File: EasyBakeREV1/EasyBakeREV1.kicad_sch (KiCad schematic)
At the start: 28 parts, among them U1 MIC5219-3.3YM5, U2 USBLC6-2SC6, U3 PCA9702, Y1 12MHz

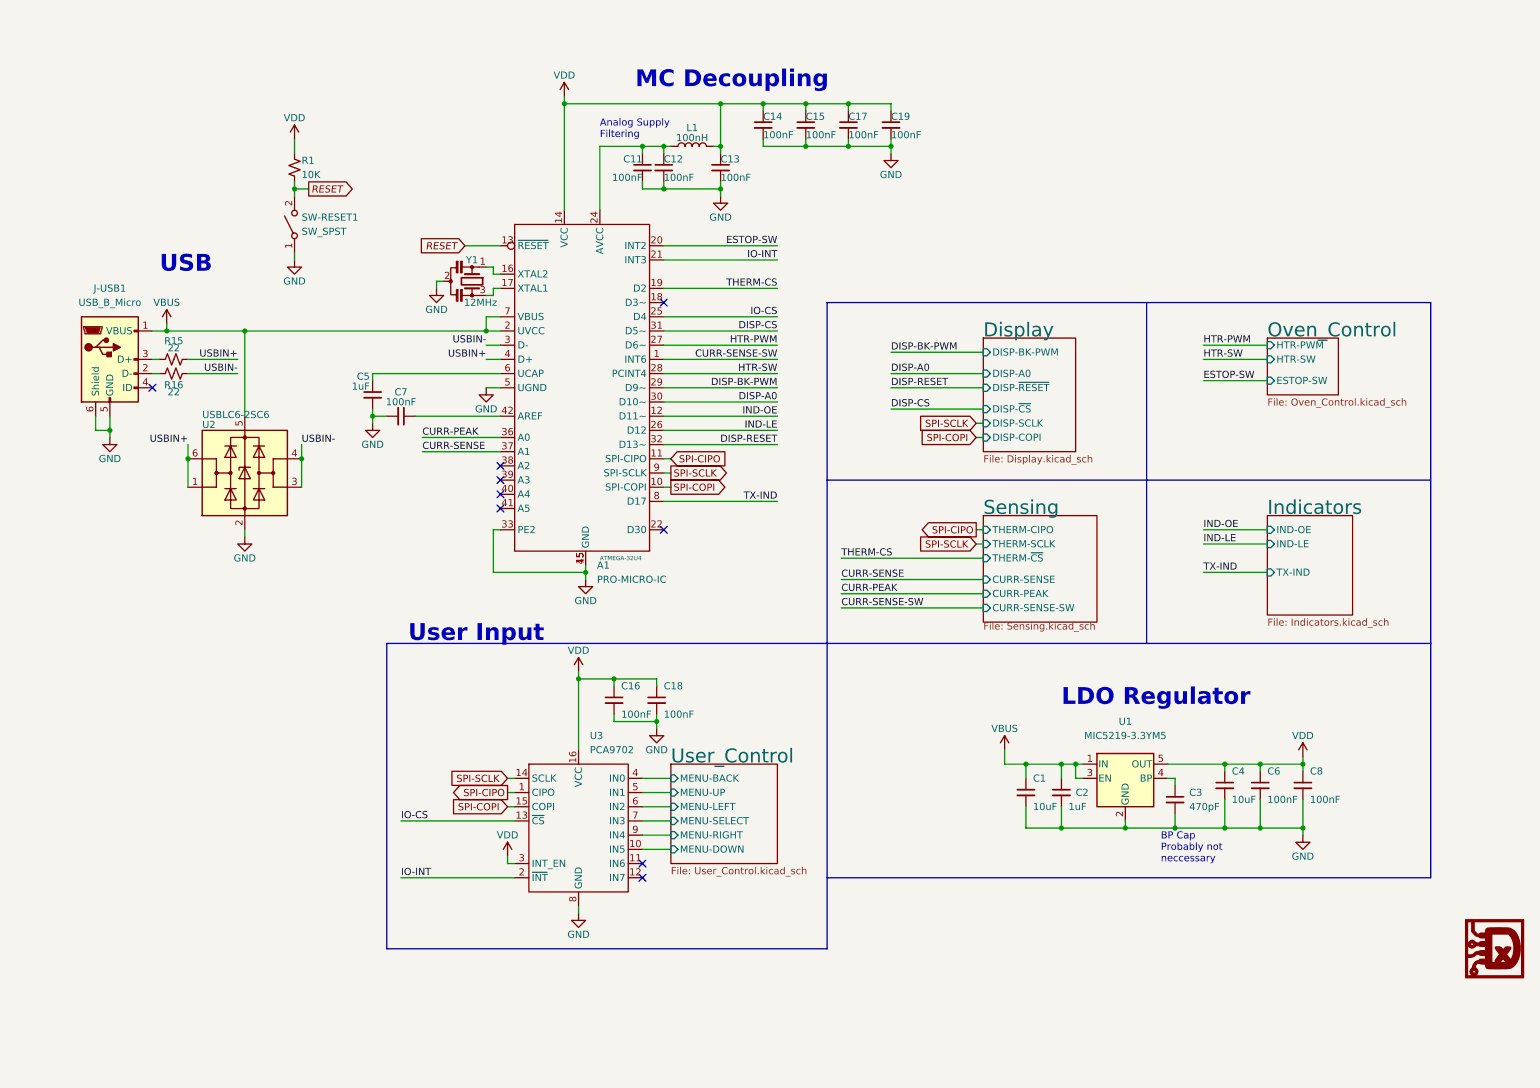
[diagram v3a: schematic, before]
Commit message: Change main pwr to 3.3 due to USB issues
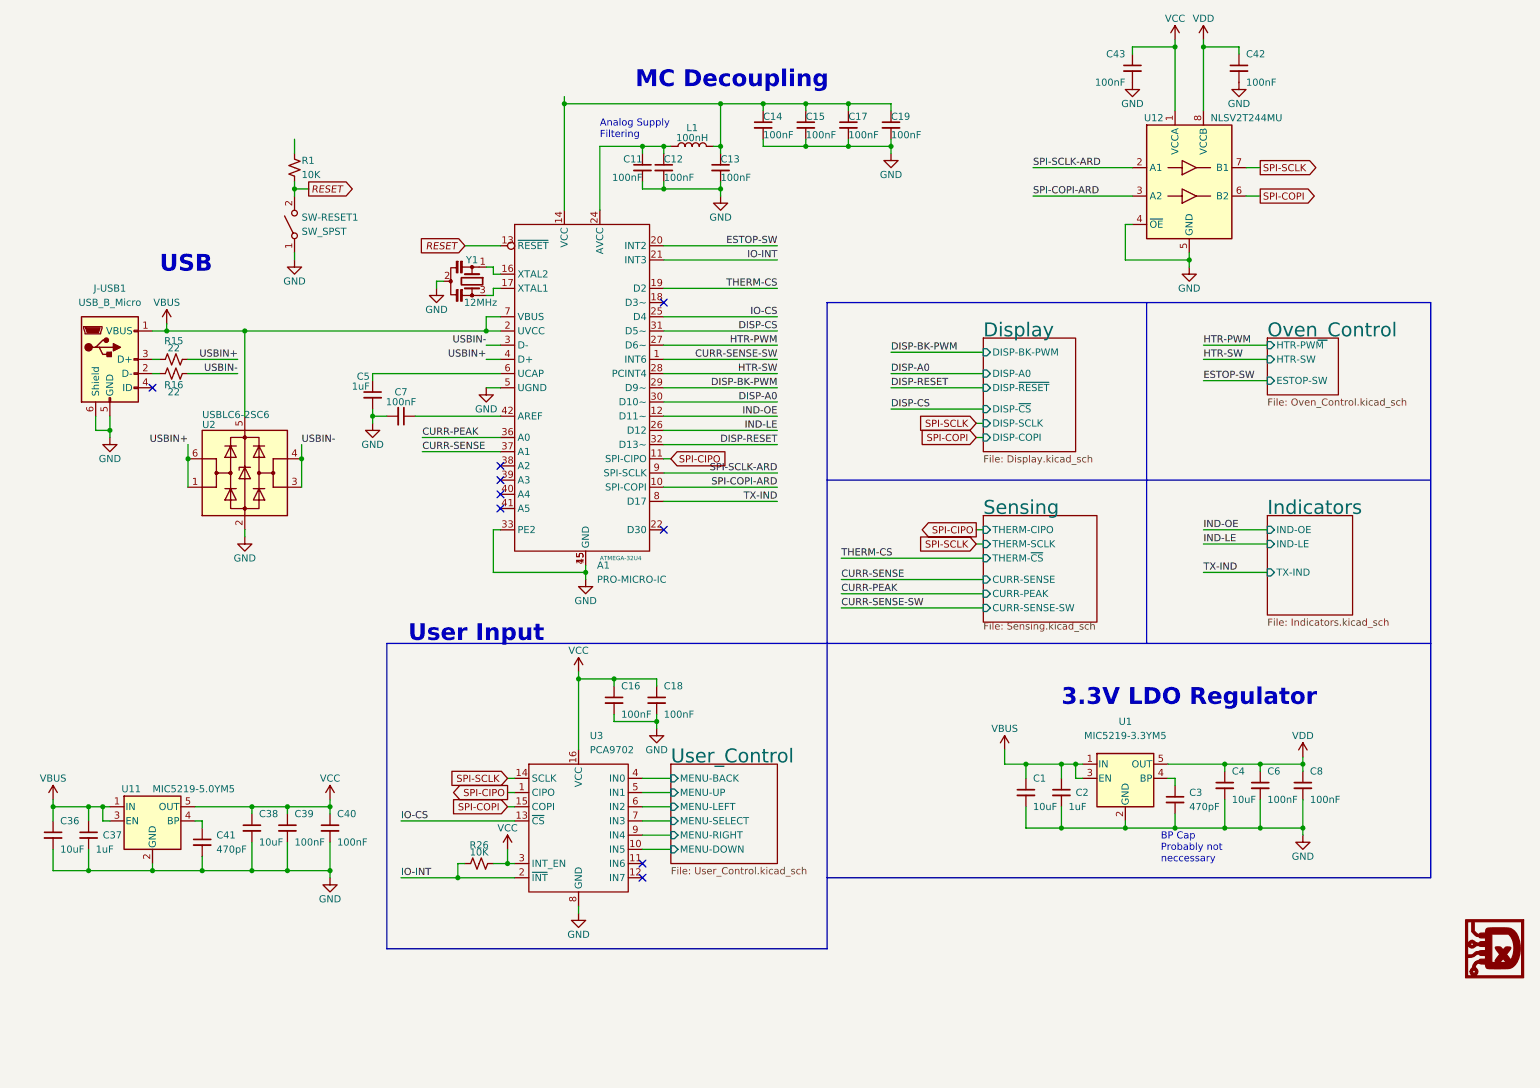
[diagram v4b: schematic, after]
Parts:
- added C36, C38: 10uF, Capacitor_SMD:C_1210_3225Metric, symbol Device:C_Small
- added C37: 1uF, Capacitor_SMD:C_1210_3225Metric, symbol Device:C_Small
- added C39, C40: 100nF, Capacitor_SMD:C_0603_1608Metric, symbol Device:C_Small
- added C41: 470pF, Capacitor_SMD:C_0603_1608Metric, symbol Device:C_Small
- added C42, C43: 100nF, Capacitor_SMD:C_0805_2012Metric, symbol Device:C_Small
- added R26: 10K, Resistor_SMD:R_0603_1608Metric, symbol Device:R_Small_US
- added U11: MIC5219-5.0YM5, Package_TO_SOT_SMD:SOT-23-5, symbol Regulator_Linear:MIC5219-5.0YM5
- added U12: NLSV2T244MU, Package_DFN_QFN:OnSemi_UDFN-8_1.2x1.8mm_P0.4mm, symbol Logic_LevelTranslator:NLSV2T244MU
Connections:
- net GND: now also C36.2, C37.2, C38.2, C39.2, C40.2, C41.2, C42.2, C43.2, U11.2 (GND), U12.4 (~{OE}), U12.5 (GND)
- net IO-INT: now also R26.1
- net SPI-COPI: now also U12.6 (B2); no longer A1.10 (PB2)
- net SPI-SCLK: now also U12.7 (B1); no longer A1.9 (PB1)
- net VBUS: now also C36.1, C37.1, U11.1 (IN), U11.3 (EN)
- net VCC: now also C38.1, C39.1, C40.1, C43.1, R26.2, U11.5 (OUT), U12.1 (VCCA); no longer C4.1, C6.1, C8.1, R1.1, U1.5 (OUT)
- new net: C41.1, U11.4 (BP)
- new net SPI-COPI-ARD: A1.10 (PB2), U12.3 (A2)
- new net SPI-SCLK-ARD: A1.9 (PB1), U12.2 (A1)
- new net VDD: C4.1, C42.1, C6.1, C8.1, U1.5 (OUT), U12.8 (VCCB)
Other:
- note added: "3.3V LDO Regulator"
- note removed: "LDO Regulator"

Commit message: Replaced MCU - started layout
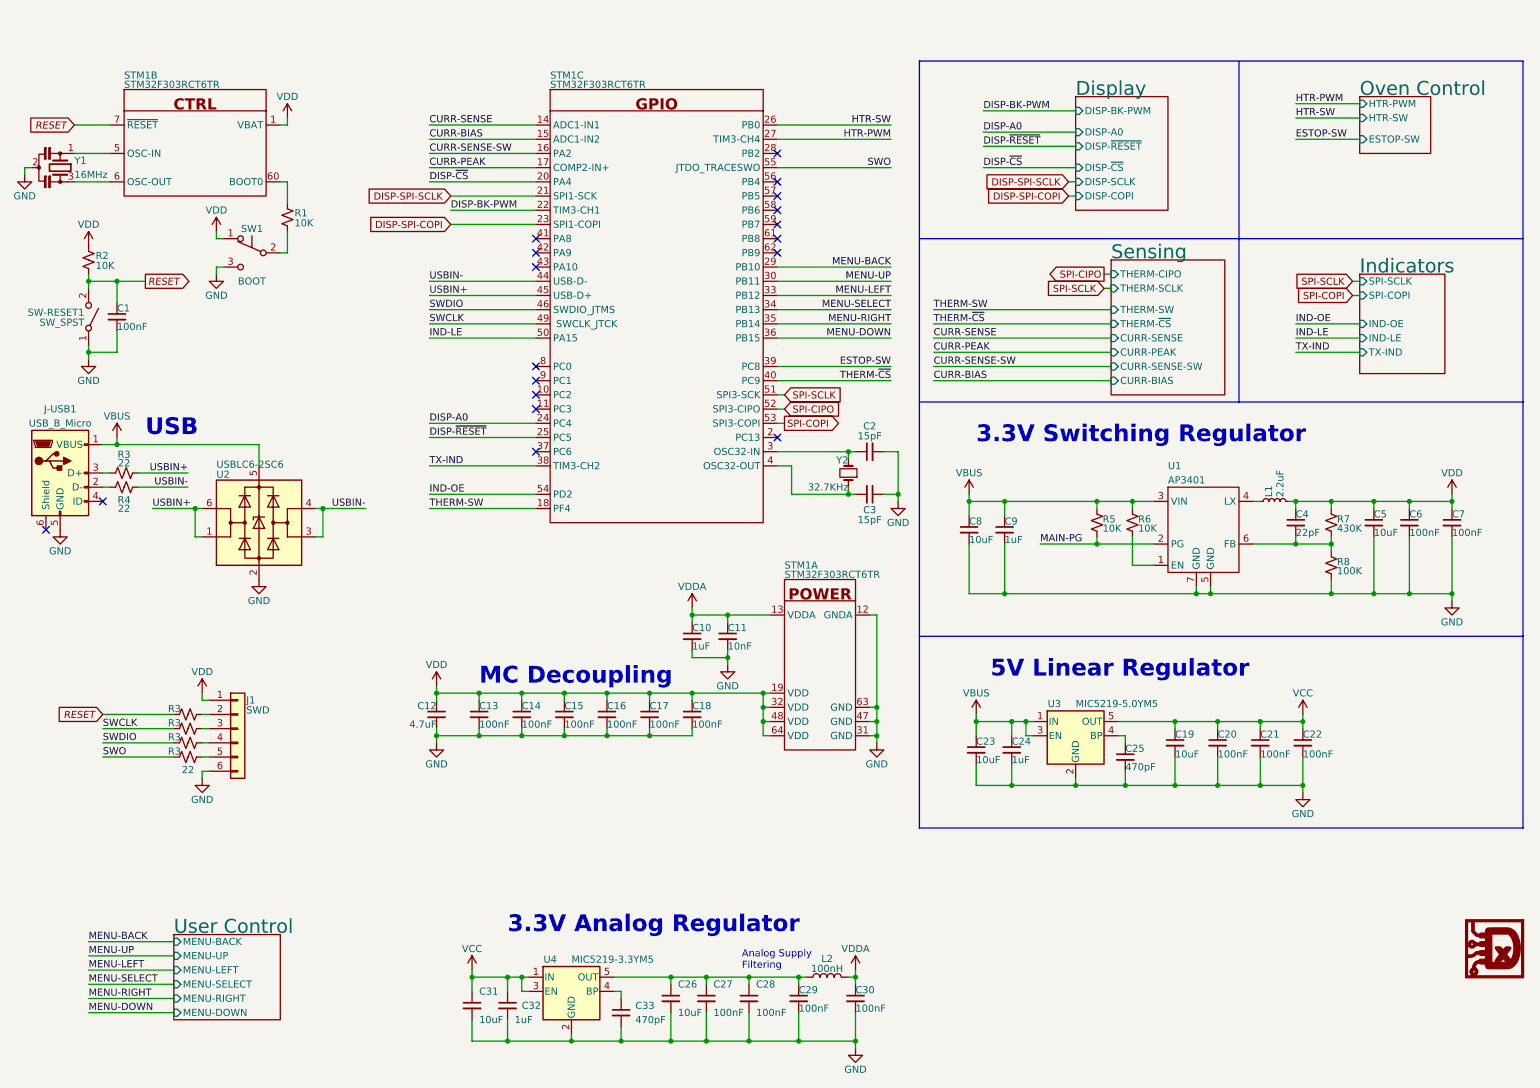
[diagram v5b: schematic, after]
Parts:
- removed A1: PRO-MICRO-IC, Daxxn_Packages:QFN-44-1EP_7x7mm_P0.5mm_EP4.8x4.8mm, symbol Daxxn_Arduino:PRO-MICRO-IC
- removed C42, C43: 100nF, Capacitor_SMD:C_0805_2012Metric, symbol Device:C_Small
- removed C5: 1uF, Capacitor_SMD:C_0805_2012Metric, symbol Device:C_Small
- removed C7: 100nF, Capacitor_SMD:C_0603_1608Metric, symbol Device:C_Small
- removed R26: 10K, Resistor_SMD:R_0603_1608Metric, symbol Device:R_Small_US
- removed U1: MIC5219-3.3YM5, Package_TO_SOT_SMD:SOT-23-5, symbol Regulator_Linear:MIC5219-3.3YM5
- removed U12: NLSV2T244MU, Package_DFN_QFN:OnSemi_UDFN-8_1.2x1.8mm_P0.4mm, symbol Logic_LevelTranslator:NLSV2T244MU
- removed U3: PCA9702, Package_SO:SSOP-16_4.4x5.2mm_P0.65mm, symbol Daxxn_IC:PCA9702
- added C1, C22, C27, C28: 100nF, Capacitor_SMD:C_0402_1005Metric, symbol Device:C_Small
- added C10, C32: 1uF, Capacitor_SMD:C_0805_2012Metric, symbol Device:C_Small
- added C12: 4.7uF, Capacitor_SMD:C_0805_2012Metric, symbol Device:C_Small
- added C2, C3: 15pF, Capacitor_SMD:C_0402_1005Metric, symbol Daxxn_Device:C
- added C26, C31: 10uF, Capacitor_SMD:C_1210_3225Metric, symbol Device:C_Small
- added C33: 470pF, Capacitor_SMD:C_0603_1608Metric, symbol Device:C_Small
- added J1: SWD, Connector_PinHeader_1.27mm:PinHeader_1x06_P1.27mm_Vertical, symbol Connector_Generic:Conn_01x06
- added L1: 2.2uF, Daxxn_Passives:LQH3NPN, symbol Daxxn_Device:L
- added R1: 10K, Resistor_SMD:R_0402_1005Metric, symbol Device:R_Small_US
- added R3 (x4): 22, Resistor_SMD:R_0402_1005Metric, symbol Device:R_Small_US
- added R5, R6: 10K, Resistor_SMD:R_0402_1005Metric, symbol Daxxn_Device:R
- added R7: 430K, Resistor_SMD:R_0402_1005Metric, symbol Daxxn_Device:R
- added R8: 100K, Resistor_SMD:R_0402_1005Metric, symbol Daxxn_Device:R
- added STM1: STM32F303RCT6TR, Package_QFP:LQFP-64_10x10mm_P0.5mm, symbol Daxxn_STMicros:STM32F303RCT6TR
- added SW1: BOOT, Daxxn_Switches:EG1218, symbol Switch:SW_Push_SPDT
- added U1: AP3401, Package_DFN_QFN:DFN-6-1EP_2x2mm_P0.65mm_EP1x1.6mm, symbol Daxxn_Regulators:AP3401
- added U4: MIC5219-3.3YM5, Package_TO_SOT_SMD:SOT-23-5, symbol Regulator_Linear:MIC5219-3.3YM5
- added Y2: 32.7KHz, Crystal:Crystal_SMD_3215-2Pin_3.2x1.5mm, symbol Daxxn_Device:Crystal_Floating
- C11: value 100nF -> 10nF; footprint Capacitor_SMD:C_0603_1608Metric -> Capacitor_SMD:C_0402_1005Metric
- C13: renamed from C16; footprint Capacitor_SMD:C_0603_1608Metric -> Capacitor_SMD:C_0402_1005Metric
- C14: renamed from C18; footprint Capacitor_SMD:C_0603_1608Metric -> Capacitor_SMD:C_0402_1005Metric
- C15: renamed from C14; footprint Capacitor_SMD:C_0603_1608Metric -> Capacitor_SMD:C_0402_1005Metric
- C16: renamed from C15; footprint Capacitor_SMD:C_0603_1608Metric -> Capacitor_SMD:C_0402_1005Metric
- C17, C6: footprint Capacitor_SMD:C_0603_1608Metric -> Capacitor_SMD:C_0402_1005Metric
- C18: renamed from C19; footprint Capacitor_SMD:C_0603_1608Metric -> Capacitor_SMD:C_0402_1005Metric
- C20: renamed from C39; footprint Capacitor_SMD:C_0603_1608Metric -> Capacitor_SMD:C_0402_1005Metric
- C21: renamed from C40; footprint Capacitor_SMD:C_0603_1608Metric -> Capacitor_SMD:C_0402_1005Metric
- C24: renamed from C37; footprint Capacitor_SMD:C_1210_3225Metric -> Capacitor_SMD:C_0805_2012Metric
- C25: renamed from C41; footprint Capacitor_SMD:C_0603_1608Metric -> Capacitor_SMD:C_0402_1005Metric
- C29: renamed from C12; footprint Capacitor_SMD:C_0603_1608Metric -> Capacitor_SMD:C_0402_1005Metric
- C30: renamed from C13; footprint Capacitor_SMD:C_0603_1608Metric -> Capacitor_SMD:C_0402_1005Metric
- C4: renamed from C3; value 470pF -> 22pF; footprint Capacitor_SMD:C_0603_1608Metric -> Capacitor_SMD:C_0402_1005Metric
- C7: renamed from C8; footprint Capacitor_SMD:C_0603_1608Metric -> Capacitor_SMD:C_0402_1005Metric
- C9: renamed from C2; footprint Capacitor_SMD:C_1210_3225Metric -> Capacitor_SMD:C_0805_2012Metric
- R2: renamed from R1; footprint Resistor_SMD:R_0603_1608Metric -> Resistor_SMD:R_0402_1005Metric
- Y1: value 12MHz -> 16MHz; footprint Crystal:Resonator_SMD_Murata_CSTxExxV-3Pin_3.0x1.1mm -> Daxxn_Passives:Resonator_SMD_3Pin_3.0x1.1mm
- renumbered C38 to C19, C36 to C23, C4 to C5, C1 to C8, L1 to L2, R15 to R3, R16 to R4, U11 to U3
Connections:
- net CURR-PEAK: now also STM1.17 (PA3)
- net CURR-SENSE: now also STM1.14 (PA0)
- net CURR-SENSE-SW: now also STM1.16 (PA2)
- net DISP-A0: now also STM1.24 (PC4)
- net DISP-BK-PWM: now also STM1.22 (PA6)
- net ESTOP-SW: now also STM1.39 (PC8)
- net GND: now also C1.2, C10.2, C12.2, C2.2, C22.2, C26.2, C27.2, C28.2, C3.1, C31.2, C32.2, C33.2, J1.6 (Pin_6), R8.2, STM1.12 (GNDA), STM1.31 (GND), STM1.47 (GND), STM1.63 (GND), SW1.3 (C), U1.5 (GND), U1.7 (GND), U4.2 (GND); no longer C4.2, J-USB1.6 (Shield)
- net HTR-PWM: now also STM1.27 (PB1)
- net HTR-SW: now also STM1.26 (PB0)
- net IND-LE: now also STM1.50 (PA15)
- net IND-OE: now also STM1.54 (PD2)
- net RESET: now also C1.1, R3.2, STM1.7 (~{RESET})
- net SPI-CIPO: now also STM1.52 (PC11)
- net SPI-COPI: now also STM1.53 (PC12)
- net SPI-SCLK: now also STM1.51 (PC10)
- net TX-IND: now also STM1.38 (PC7)
- net USBIN+: now also STM1.45 (PA12)
- net USBIN-: now also STM1.44 (PA11)
- net VBUS: now also R5.1, R6.1, U1.3 (VIN)
- net VCC: now also C22.1, C31.1, C32.1, U4.1 (IN), U4.3 (EN); no longer C13.1, C14.1, C15.1, C16.1, C17.1, C18.1, C30.1, L2.2
- net VDD: now also C13.1, C14.1, C15.1, C16.1, C17.1, C18.1, C4.1, R2.1, C12.1, J1.1 (Pin_1), L1.2, R7.1, STM1.1 (VBAT), STM1.19 (VDD), STM1.32 (VDD), STM1.48 (VDD), STM1.64 (VDD), SW1.1 (A)
- net at Y1.1: now also STM1.5 (OSC-IN)
- net at Y1.3: now also STM1.6 (OSC-OUT)
- net AVCC: no longer names the net of C29.1, L2.1
- net AVCC: now also C26.1, C27.1, C28.1, U4.5 (OUT); no longer C11.1
- new net: R1.1, STM1.60 (BOOT0)
- new net: C2.1, STM1.3 (PC14), Y2.2
- new net: C3.2, STM1.4 (PC15), Y2.1
- new net: C4.2, R7.2, R8.1, U1.6 (FB)
- new net: C33.1, U4.4 (BP)
- new net: J1.5 (Pin_5), R3.1
- new net: R1.2, SW1.2 (B)
- new net: J1.2 (Pin_2), R3.1
- new net: J1.3 (Pin_3), R3.1
- new net: J1.4 (Pin_4), R3.1
- new net: R6.2, U1.1 (EN)
- new net: L1.1, U1.4 (LX)
- new net CURR-BIAS: STM1.15 (PA1)
- new net DISP-SPI-COPI: STM1.23 (PA7)
- new net DISP-SPI-SCLK: STM1.21 (PA5)
- new net DISP-~{CS}: STM1.20 (PA4)
- new net DISP-~{RESET}: STM1.25 (PC5)
- new net MAIN-PG: R5.2, U1.2 (PG)
- new net MENU-BACK: STM1.29 (PB10)
- new net MENU-DOWN: STM1.36 (PB15)
- new net MENU-LEFT: STM1.33 (PB12)
- new net MENU-RIGHT: STM1.35 (PB14)
- new net MENU-SELECT: STM1.34 (PB13)
- new net MENU-UP: STM1.30 (PB11)
- new net SWCLK: R3.2, STM1.49 (PA14)
- new net SWDIO: R3.2, STM1.46 (PA13)
- new net SWO: R3.2, STM1.55 (PB3)
- new net THERM-SW: STM1.18 (PF4)
- new net THERM-~{CS}: STM1.40 (PC9)
- new net VDDA: C10.1, C11.1, C30.1, L2.2, STM1.13 (VDDA)
- no-connect marks 9 -> 18
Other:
- sheet Oven_Control renamed Oven Control
- sheet User_Control renamed User Control
- sheet Indicators ports: added SPI-COPI, SPI-SCLK; removed none
- sheet Sensing ports: added CURR-BIAS, THERM-SW; removed none
- note added: "3.3V Analog Regulator"
- note added: "3.3V Switching Regulator"
- note added: "5V Linear Regulator"
- note removed: "3.3V LDO Regulator"
- note removed: "BP Cap Probably not neccessary"
- note removed: "User Input"
- moved on the sheet: C11, C13, C14, C15, C16, C17, C18, C19, C20, C21, C23, C24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

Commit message: Rearrange footprints and start layout
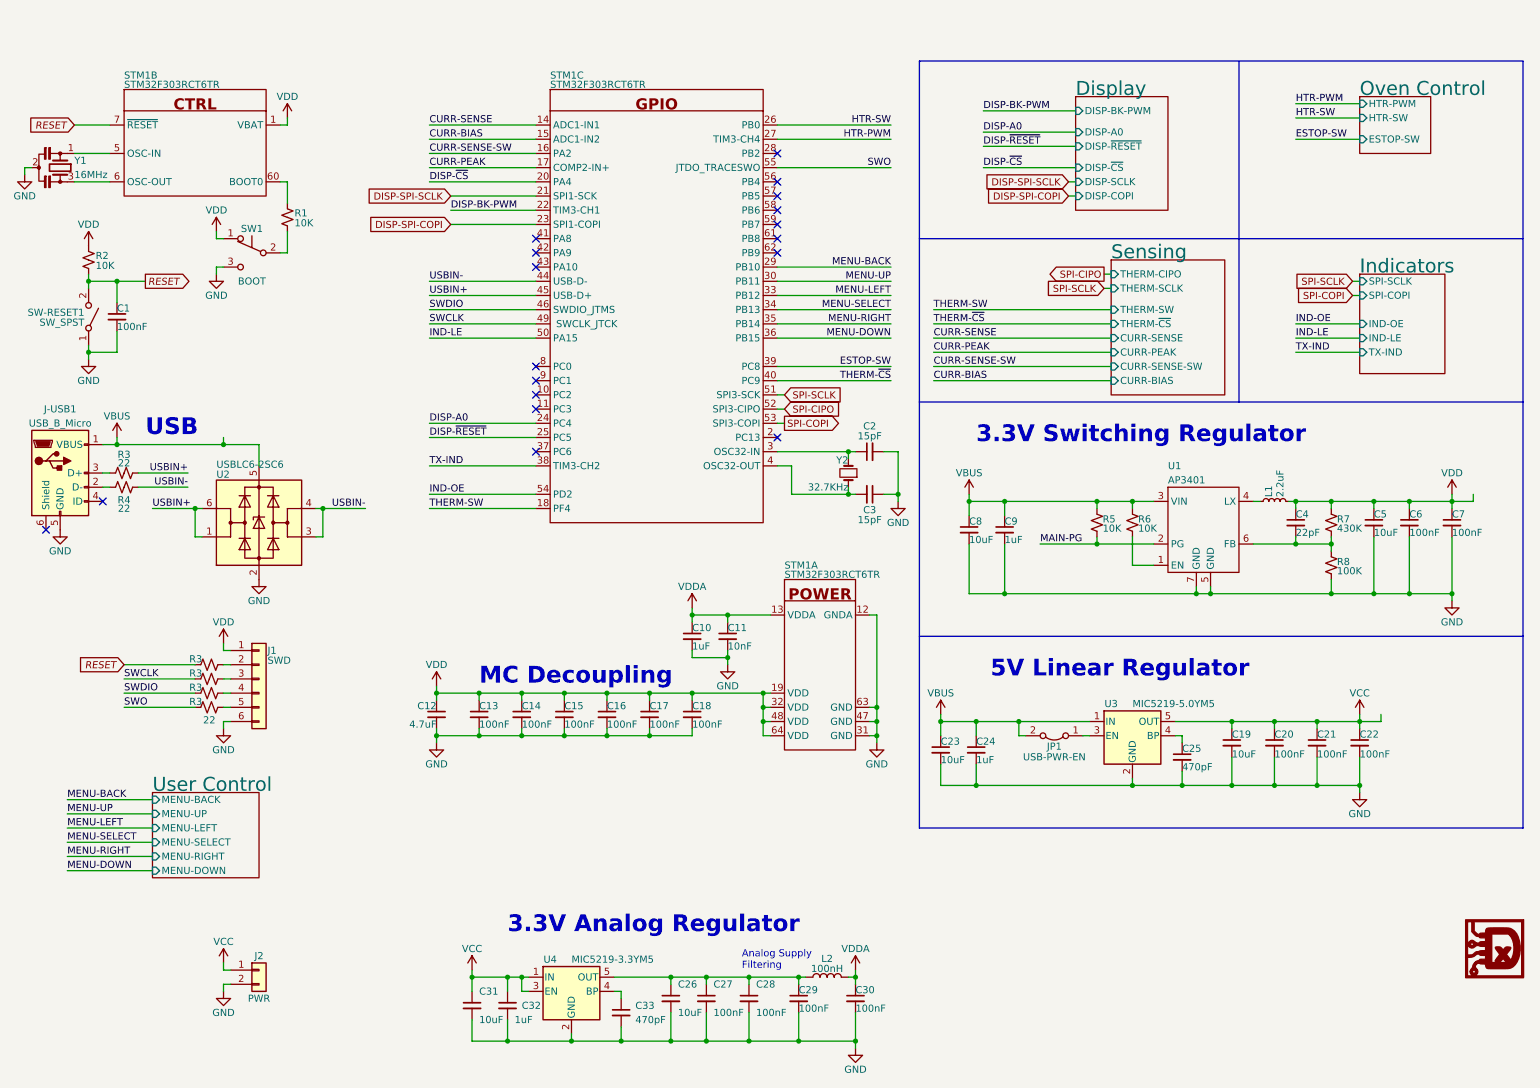
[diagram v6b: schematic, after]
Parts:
- added J2: PWR, Connector_PinHeader_2.54mm:PinHeader_1x02_P2.54mm_Vertical, symbol Connector_Generic:Conn_01x02
- added JP1: USB-PWR-EN, Jumper:SolderJumper-2_P1.3mm_Open_RoundedPad1.0x1.5mm, symbol Jumper:Jumper_2_Bridged
- Y2: footprint Crystal:Crystal_SMD_3215-2Pin_3.2x1.5mm -> Daxxn_Passives:Crystal_SMD_3215-2Pin_3.2x1.5mm
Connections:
- net GND: now also J2.2 (Pin_2)
- net VBUS: now also JP1.2 (B); no longer U3.3 (EN)
- net VCC: now also J2.1 (Pin_1)
- new net: JP1.1 (A), U3.3 (EN)
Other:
- moved on the sheet: C19, C20, C21, C22, C23, C24, C25, J1, R3, U3
